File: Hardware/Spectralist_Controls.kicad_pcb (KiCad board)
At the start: 2 copper layers, 60 x 110 mm, 30 parts, among them J1 Conn_01x8_Pin, J10 FilterA_CV, J11 FilterB_CV, J12 ChannelAOut, J13 ChannelBOut, J14 SlopeCV, J15 Conn_01x02_Pin, J16 Conn_01x02_Pin, J2 Conn_01x8_Pin, J3 Conn_01x10_Pin, J4 Conn_01x10_Pin, J5 StretchCV, J6 VOctCV, J7 WarpCV, J8 PanCV, J9 Conn_01x03_Pin, SW1 Harmonic_Switch, SW2 Filter_Switch, SW3 B_Octave

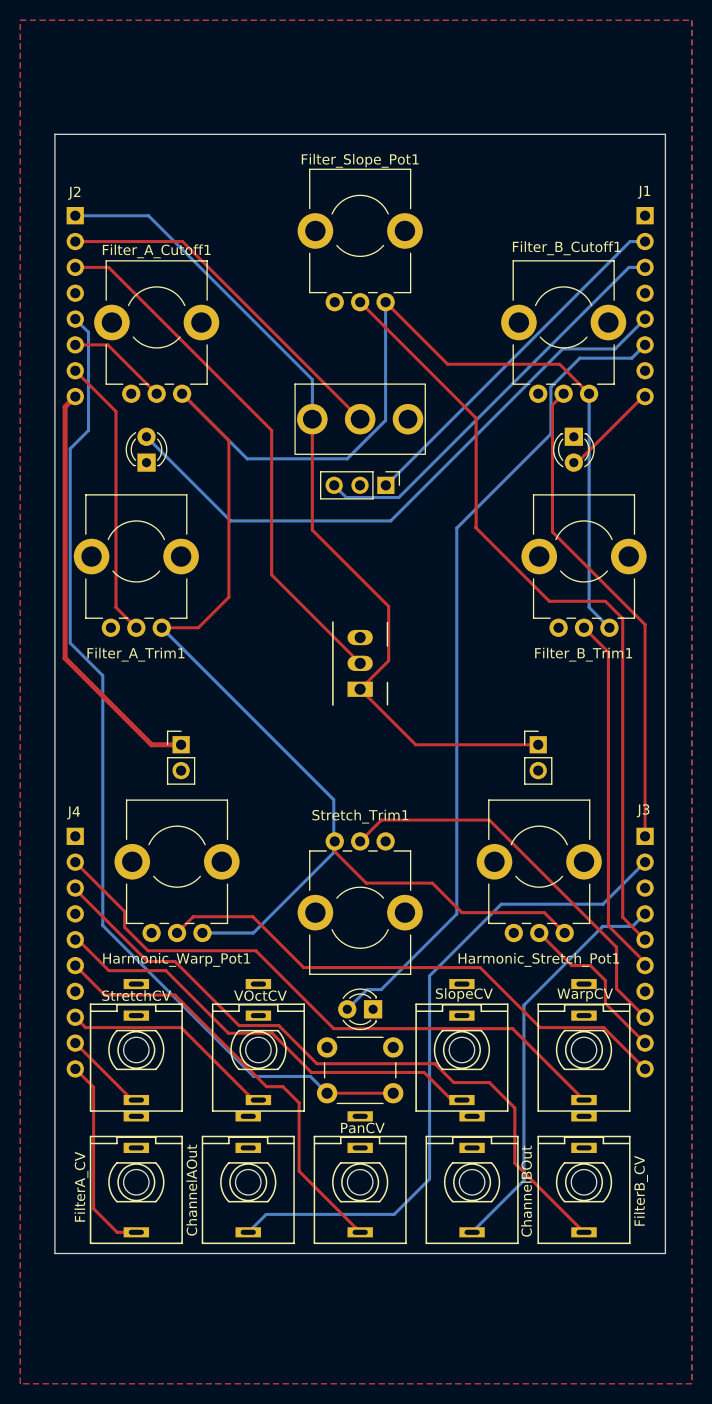
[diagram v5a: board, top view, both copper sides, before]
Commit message: Started adding JLC part numbers
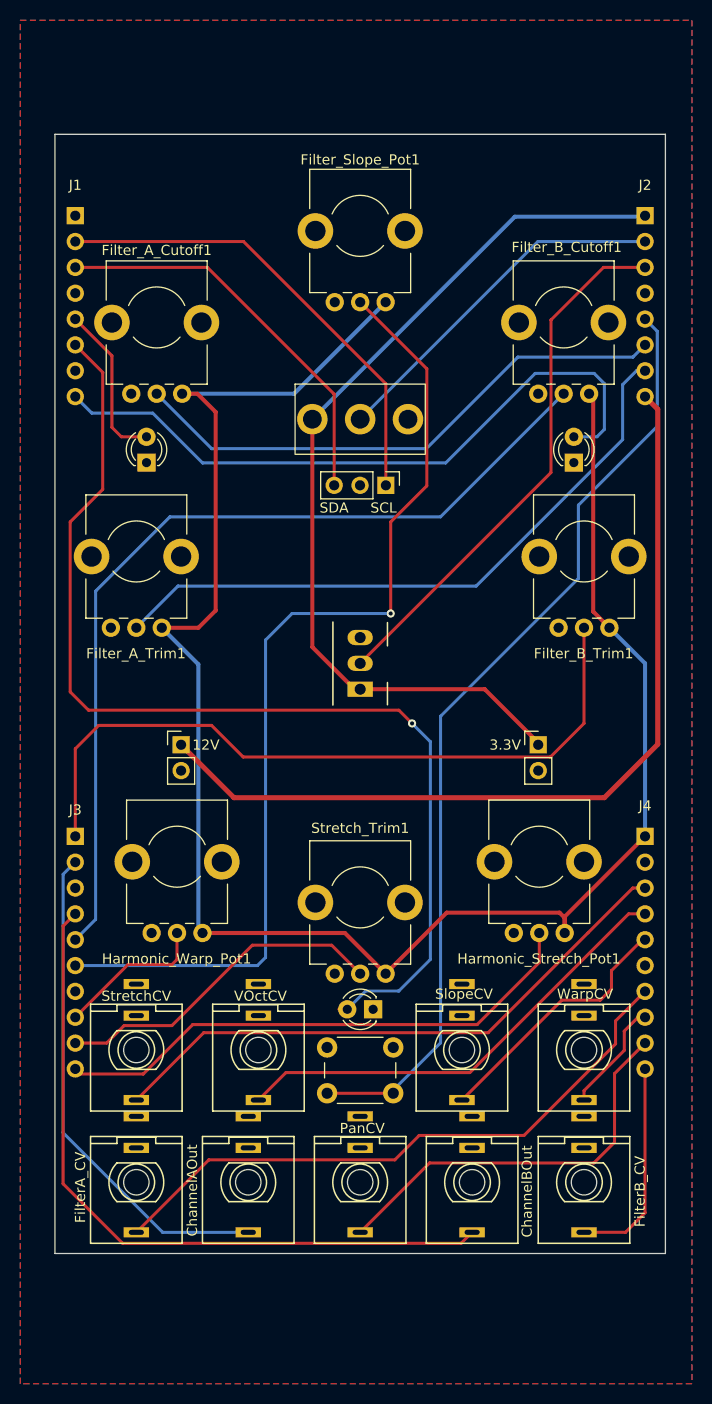
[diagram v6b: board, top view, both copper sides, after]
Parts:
- J1, J2: footprint Connector_PinHeader_2.54mm:PinHeader_1x08_P2.54mm_Vertical -> Connector_PinSocket_2.54mm:PinSocket_1x08_P2.54mm_Vertical
- J3, J4: footprint Connector_PinHeader_2.54mm:PinHeader_1x10_P2.54mm_Vertical -> Connector_PinSocket_2.54mm:PinSocket_1x10_P2.54mm_Vertical
- moved J1 56.0 mm to (102.0, 58.0)
- moved J2 56.0 mm to (158.0, 58.0)
- moved J3 56.0 mm to (102.0, 119.0)
- moved J4 56.0 mm to (158.0, 119.0)
- moved Stretch_Trim1 2.00 mm to (130.0, 125.0), turned to 0 degrees
- turned D2 to 90 degrees
- renumbered J9 to J14, J14 to J9
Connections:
- J3 pad 1: /Filter_B_Pot -> /Filter_B_Trm
- J3 pad 10: /Harm_Warp_Pot -> /Harm_Stretch_Pot
- J3 pad 5: /Filter_Slope_Pot -> /Filter_B_Pot
- J3 pad 6: /Filter_B_Trm -> /Filter_Slope_Pot
- J3 pad 8: /Harm_Stretch_Trm -> /Harm_Warp_Pot
- J3 pad 9: /Harm_Stretch_Pot -> /Harm_Stretch_Trm
- J4 pad 1: GND -> +3.3VA
- J4 pad 10: /Filter_A_CV_In -> /Filter_B_CV_In
- J4 pad 2: /Harm_Warp_CV_In -> GND
- J4 pad 3: /Filter_B_CV_In -> /Harm_Stretch_CV_In
- J4 pad 4: GND -> /Pitch_CV_In
- J4 pad 6: /Pan_CV_In -> GND
- J4 pad 7: GND -> /Filter_A_CV_In
- J4 pad 8: /Pitch_CV_In -> /Harm_Warp_CV_In
- J4 pad 9: /Harm_Stretch_CV_In -> /Pan_CV_In
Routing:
- net /LED_Filter_B_Out: track 9.69 -> 66.6 mm
- net /Harm_Stretch_CV_In: track 8.32 -> 58.6 mm
- net /Harm_Warp_CV_In: track 60.6 -> 11.3 mm
- net /Filter_B_CV_In: track 67.3 -> 20.9 mm
- net +12V: track 41.1 -> 85.9 mm
- net /LED_Filter_A_Out: track 60.6 -> 15.9 mm
- net /Filter_A_Pot: track 9.99 -> 54.5 mm
- net /Filter_A_CV_In: track 19.6 -> 61.1 mm
- net /Filter_B_Pot: track 47.7 -> 89.1 mm
- net /Harm_Warp_Pot: track 52.9 -> 15.0 mm
- net /Harm_Stretch_Pot: track 16.2 -> 53.2 mm
- net /Filter_B_Trm: track 35.7 -> 71.6 mm
- net /Filter_A_Trm: track 27.7 -> 63.6 mm
- net /Audio_Out_R: track 40.1 -> 70.1 mm
- net /LED_Oct_Out: track 81.2 -> 106.4 mm, vias 0 -> 1
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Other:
- board text added: "12V"
- board text added: "3.3V"
- board text added: "Mountjoy Modular 2025 Spectralist Controls v1.0"
- board text added: "SCL"
- board text added: "SDA"
- board text removed: "Mountjoy Modular 2024 Spectralist Controls v1.0"

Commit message: v1.0 PCBs sent to production
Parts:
- moved Harmonic_Stretch_Pot1 2.40 mm to (150.0, 121.0)
- moved Harmonic_Warp_Pot1 2.00 mm to (110.0, 121.0)
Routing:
- net /LED_Oct_Out: track 106.4 -> 91.1 mm
- net +3.3VA: track 184.9 -> 188.7 mm
- net /Harm_Warp_Pot: track 15.0 -> 11.6 mm
- net /Filter_Slope_Pot: track 98.4 -> 96.1 mm
- net /Pan_CV_In: track 39.7 -> 37.8 mm
- net /Harm_Stretch_CV_In: track 58.6 -> 60.2 mm
- net /Pitch_CV_In: track 45.6 -> 46.8 mm
- net /Harm_Stretch_Pot: track 53.2 -> 54.2 mm
- net /Harm_Stretch_Trm: track 33.1 -> 32.3 mm
- net GND: vias 0 -> 22

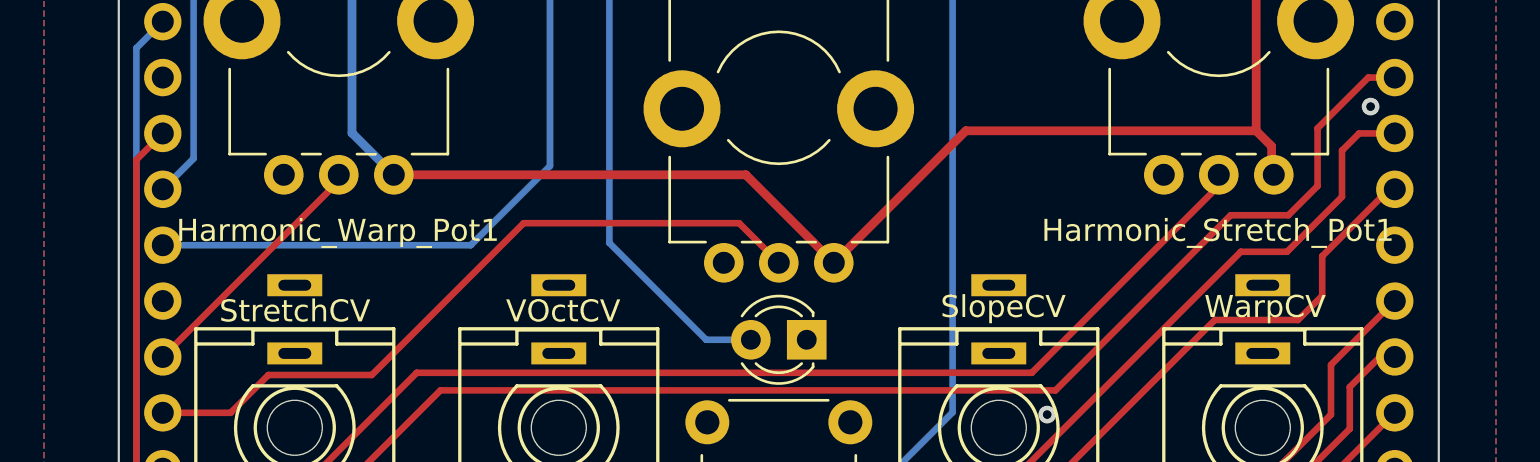
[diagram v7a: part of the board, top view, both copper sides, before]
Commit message: Code tidy up; implementing CV , pots and trimmers
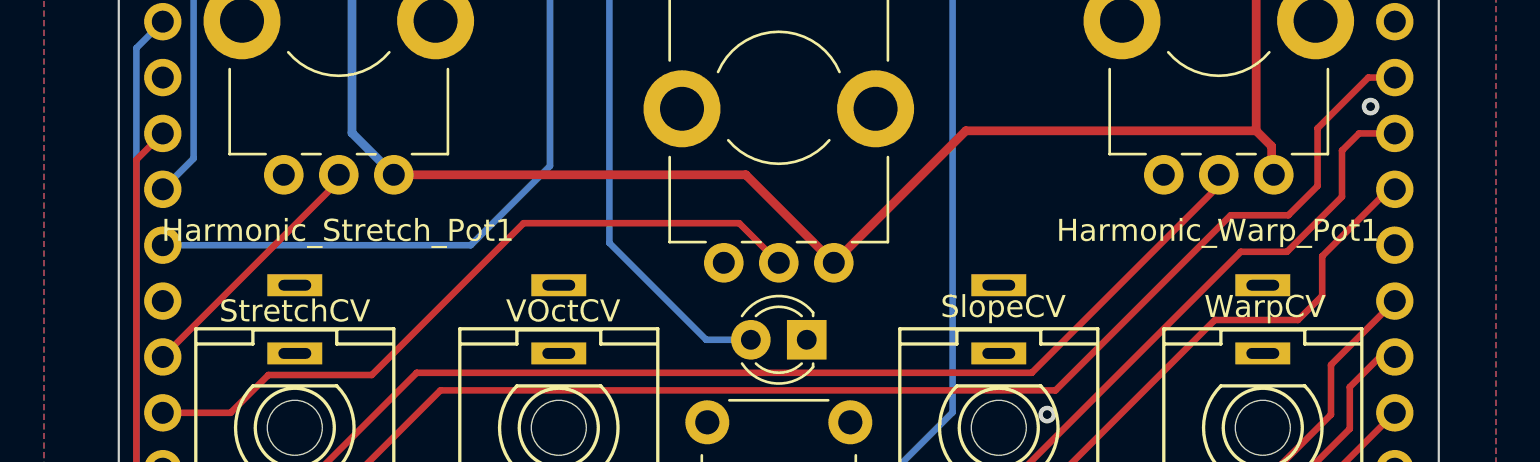
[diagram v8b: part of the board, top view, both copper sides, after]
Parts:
- renumbered Harmonic_Warp_Pot1 to Harmonic_Stretch_Pot1, Harmonic_Stretch_Pot1 to Harmonic_Warp_Pot1
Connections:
- Harmonic_Stretch_Pot1 pad 2: /Harm_Warp_Pot -> /Harm_Stretch_Pot
- Harmonic_Warp_Pot1 pad 2: /Harm_Stretch_Pot -> /Harm_Warp_Pot
- J3 pad 10: /Harm_Stretch_Pot -> /Harm_Warp_Pot
- J3 pad 8: /Harm_Warp_Pot -> /Harm_Stretch_Pot
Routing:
- net /Harm_Warp_Pot: track 11.6 -> 54.2 mm
- net /Harm_Stretch_Pot: track 54.2 -> 11.6 mm
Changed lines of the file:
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@@
 		(descr "Potentiometer 9mm")
 		(tags "Potentiometer 9mm")
-		(property "Reference" "Harmonic_Warp_Pot1"
+		(property "Reference" "Harmonic_Stretch_Pot1"
 			(at -0.04 10.04 0)
 			(layer "F.SilkS")
@@
 			(layers "*.Cu" "*.Mask")
 			(remove_unused_layers no)
-			(net 23 "/Harm_Warp_Pot")
+			(net 26 "/Harm_Stretch_Pot")
 			(pinfunction "2")
 			(pintype "passive")
@@
 		(descr "Potentiometer 9mm")
 		(tags "Potentiometer 9mm")
-		(property "Reference" "Harmonic_Stretch_Pot1"
+		(property "Reference" "Harmonic_Warp_Pot1"
 			(at -0.04 10.04 0)
 			(layer "F.SilkS")
@@
 			(layers "*.Cu" "*.Mask")
 			(remove_unused_layers no)
-			(net 26 "/Harm_Stretch_Pot")
+			(net 23 "/Harm_Warp_Pot")
 			(pinfunction "2")
 			(pintype "passive")
@@
 			(layers "*.Cu" "*.Mask")
 			(remove_unused_layers no)
-			(net 23 "/Harm_Warp_Pot")
+			(net 26 "/Harm_Stretch_Pot")
 			(pinfunction "Pin_8")
 			(pintype "passive")
@@
 			(layers "*.Cu" "*.Mask")
 			(remove_unused_layers no)
-			(net 26 "/Harm_Stretch_Pot")
+			(net 23 "/Harm_Warp_Pot")
 			(pinfunction "Pin_10")
 			(pintype "passive")
@@
 	)
 	(segment
-		(start 110 128.5)
-		(end 110 128.78)
+		(start 102 141.86)
+		(end 102.5 142.36)
 		(width 0.3)
 		(layer "F.Cu")
@@
 	)
 	(segment
-		(start 110 128.78)
-		(end 102 136.78)
+		(start 108.680559 142.36)
+		(end 113.540559 137.5)
+		(width 0.3)
+		(layer "F.Cu")
+		(net 23)
+	)
+	(segment
+		(start 102.5 142.36)
+		(end 108.680559 142.36)
+		(width 0.3)
+		(layer "F.Cu")
+		(net 23)
+	)
+	(segment
+		(start 150 129)
+		(end 150 128.5)
+		(width 0.3)
+		(layer "F.Cu")
+		(net 23)
+	)
+	(segment
+		(start 141.5 137.5)
+		(end 150 129)
+		(width 0.3)
+		(layer "F.Cu")
+		(net 23)
+	)
+	(segment
+		(start 113.540559 137.5)
+		(end 141.5 137.5)
 		(width 0.3)
 		(layer "F.Cu")
@@
 	)
 	(segment
-		(start 102 141.86)
-		(end 102.5 142.36)
-		(width 0.3)
-		(layer "F.Cu")
-		(net 26)
-	)
-	(segment
-		(start 108.680559 142.36)
-		(end 113.540559 137.5)
-		(width 0.3)
-		(layer "F.Cu")
-		(net 26)
-	)
-	(segment
-		(start 102.5 142.36)
-		(end 108.680559 142.36)
-		(width 0.3)
-		(layer "F.Cu")
-		(net 26)
-	)
-	(segment
-		(start 150 129)
-		(end 150 128.5)
-		(width 0.3)
-		(layer "F.Cu")
-		(net 26)
-	)
-	(segment
-		(start 141.5 137.5)
-		(end 150 129)
+		(start 110 128.5)
+		(end 110 128.78)
 		(width 0.3)
 		(layer "F.Cu")
@@
 	)
 	(segment
-		(start 113.540559 137.5)
-		(end 141.5 137.5)
+		(start 110 128.78)
+		(end 102 136.78)
 		(width 0.3)
 		(layer "F.Cu")
